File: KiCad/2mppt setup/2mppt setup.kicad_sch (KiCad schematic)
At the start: 3 parts

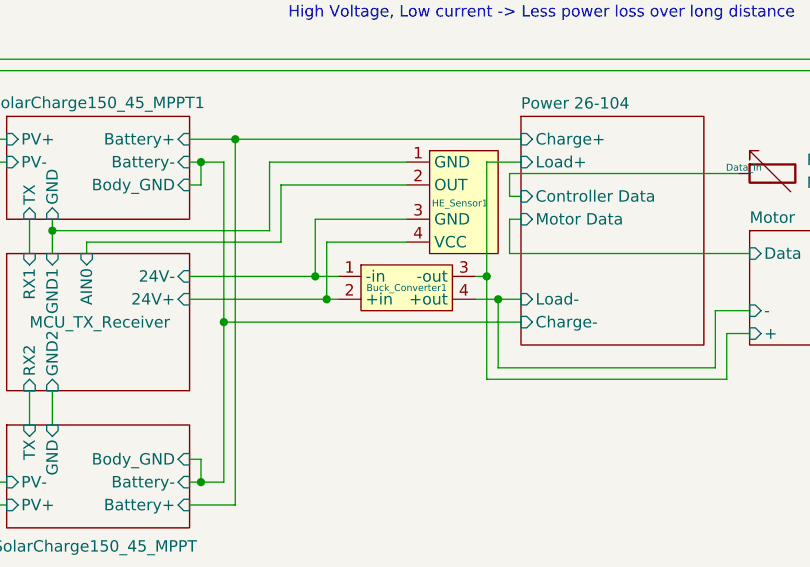
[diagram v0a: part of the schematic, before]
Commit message: Fix wiring check issue
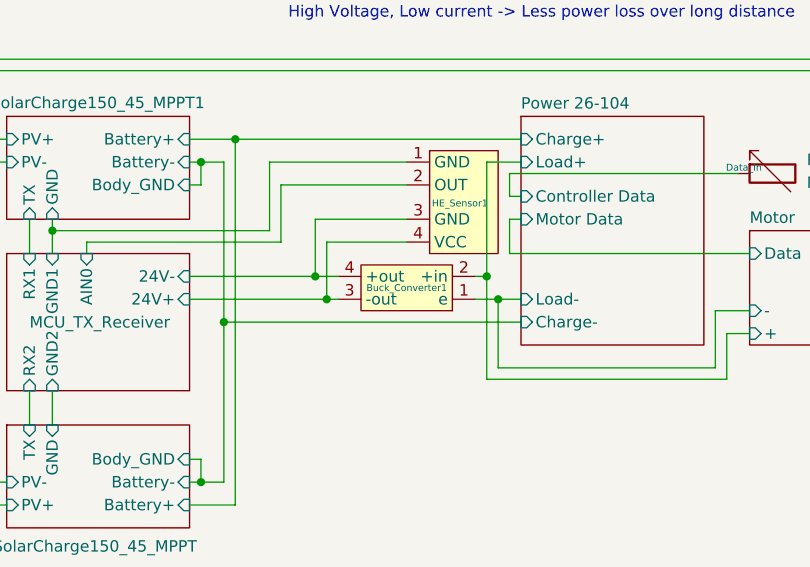
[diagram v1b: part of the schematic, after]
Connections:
- net MCU_TX_Receiver/24V+: now also Buck_Converter1.3 (-out); no longer Buck_Converter1.2 (+in)
- net MCU_TX_Receiver/24V-: now also Buck_Converter1.4 (+out); no longer Buck_Converter1.1 (-in)
- net Motor/+: now also Buck_Converter1.2 (+in); no longer Buck_Converter1.3 (-out)
- net Motor/-: now also Buck_Converter1.1 (e); no longer Buck_Converter1.4 (+out)
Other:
- moved on the sheet: Buck_Converter1
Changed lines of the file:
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@@
 	(symbol
 		(lib_id "Proa:DC-DC_Buck_Converter")
-		(at 140.97 69.85 0)
+		(at 138.43 69.85 180)
 		(unit 1)
 		(exclude_from_sim no)
@@
 		)
 		(property "Value" "~"
-			(at 139.446 69.85 0)
+			(at 139.954 69.85 0)
 			(effects
 				(font
@@
 		)
 		(property "Footprint" ""
-			(at 143.51 68.58 0)
+			(at 135.89 71.12 0)
 			(effects
 				(font
@@
 		)
 		(property "Datasheet" ""
-			(at 143.51 68.58 0)
+			(at 135.89 71.12 0)
 			(effects
 				(font
@@
 		)
 		(property "Description" ""
-			(at 143.51 68.58 0)
+			(at 135.89 71.12 0)
 			(effects
 				(font

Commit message: KiCad_Skip & Schemdraw test
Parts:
- removed Buck_Converter1: ~, symbol Proa:DC-DC_Buck_Converter
- added SW1: 100A Main Switch, symbol Switch:SW_DIP_x02
- added U3: BUCK_48V_24V_?A, symbol Proa:BUCK_48V_24V_?A
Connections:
- net MCU_TX_Receiver/24V+: now also U3.3 (Vout+)
- net MCU_TX_Receiver/24V-: now also U3.4 (Vout-)
- net Motor/+: now also SW1.2, U3.1 (Vin+)
- net Motor/-: now also U3.2 (Vin-)
- net Power 26-104/Charge+: now also SW1.4
- new net Power 26-104/Load+: SW1.3
- new net SolarCharge150_45_MPPT/Battery+: SW1.1
- no-connect marks 0 -> 2
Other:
- added sheet Smaller batteries in series (BatteryArray.kicad_sch)
- note added: "Plug"
- moved on the sheet: HE_Sensor1, R1
